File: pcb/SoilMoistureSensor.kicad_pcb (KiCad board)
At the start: 2 copper layers, 41.4 x 72 mm, 15 parts, among them J1 Conn_01x03_Male, M2 MountingHole_2.2mm_M2_Pad_Via, Q1 2N2222, U1 ESP-12E

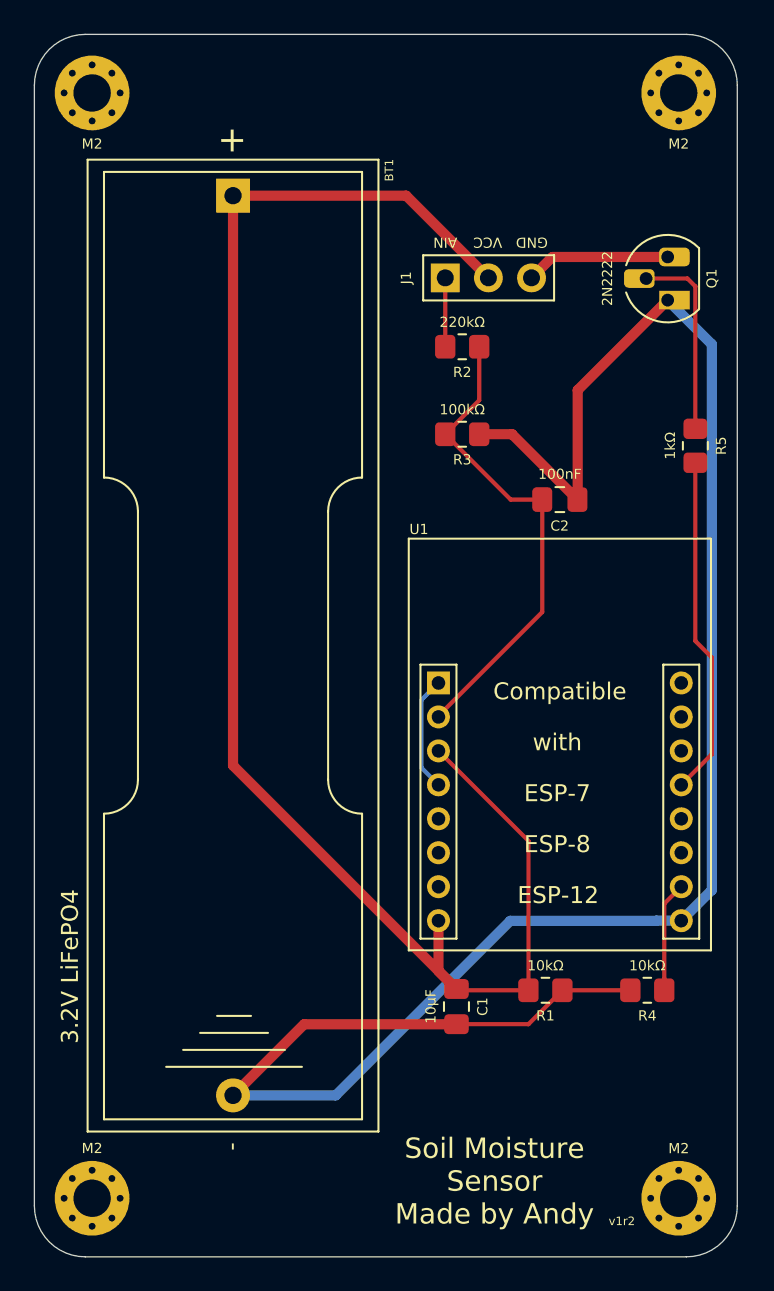
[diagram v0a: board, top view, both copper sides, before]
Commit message: PCB v1r3: Made it 40mm width again, as it fits perfectly in old tomato sauce glasses ;)
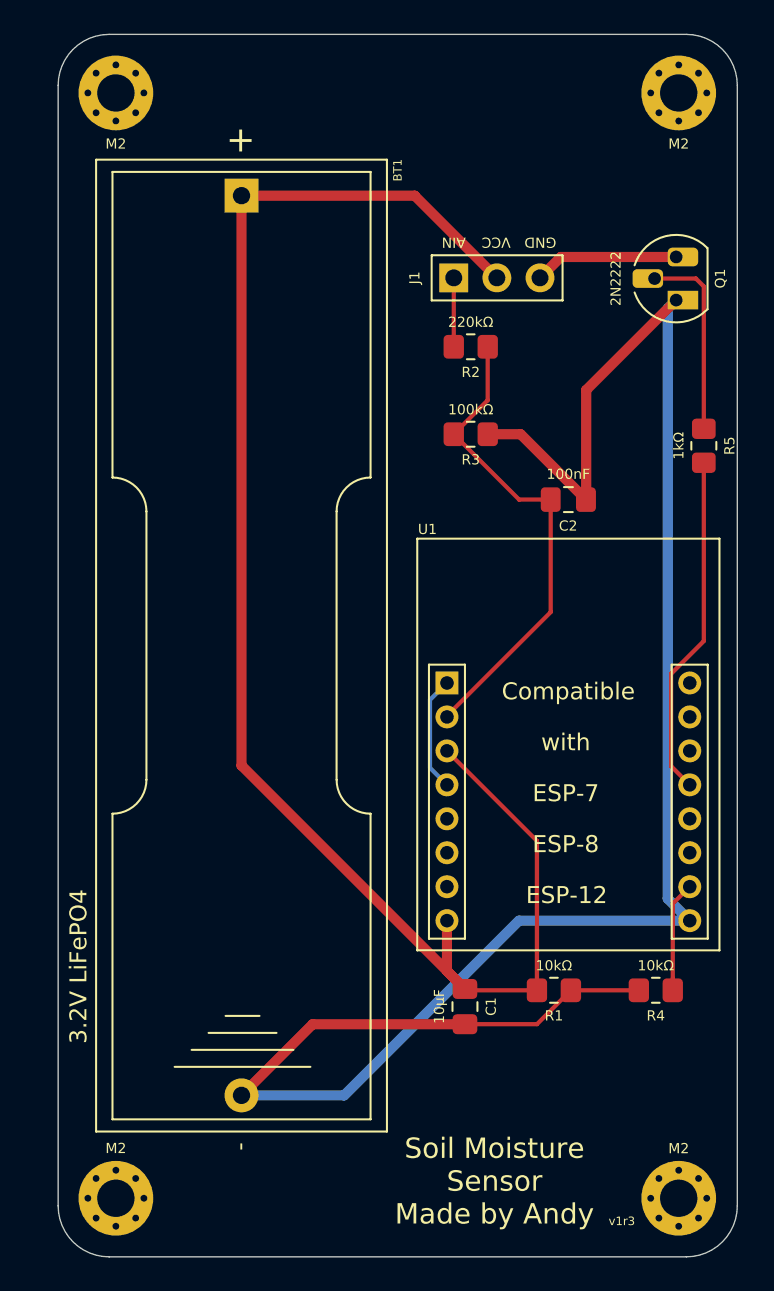
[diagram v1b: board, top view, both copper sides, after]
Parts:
- moved M2 1.40 mm to (138.4, 83.5)
- moved M2 1.40 mm to (138.4, 148.6)
- moved BT1 0.50 mm to (145.8, 90.0)
- moved C1 0.50 mm to (159.0, 137.3)
- moved C2 0.50 mm to (165.1, 107.4)
- moved J1 0.50 mm to (158.3, 94.3)
- moved Q1 0.50 mm to (171.4, 95.7)
- moved R1 0.50 mm to (164.2, 136.3)
- moved R2 0.50 mm to (159.3, 98.4)
- moved R3 0.50 mm to (159.3, 103.5)
- moved R4 0.50 mm to (170.2, 136.3)
- moved R5 0.50 mm to (173.0, 104.2)
- moved U1 0.50 mm to (157.9, 118.2)
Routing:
- net /GND: track 116.3 -> 115.3 mm
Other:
- board size 41.4 x 72 mm -> 40 x 72 mm
- board text added: "v1r3"
- board text removed: "v1r2"
